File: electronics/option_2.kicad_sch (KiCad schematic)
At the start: 11 parts, among them Q6 Q_PMOS_GSD, U19 LM339_4ch, U20 LM339_4ch, U5 ULN2801A

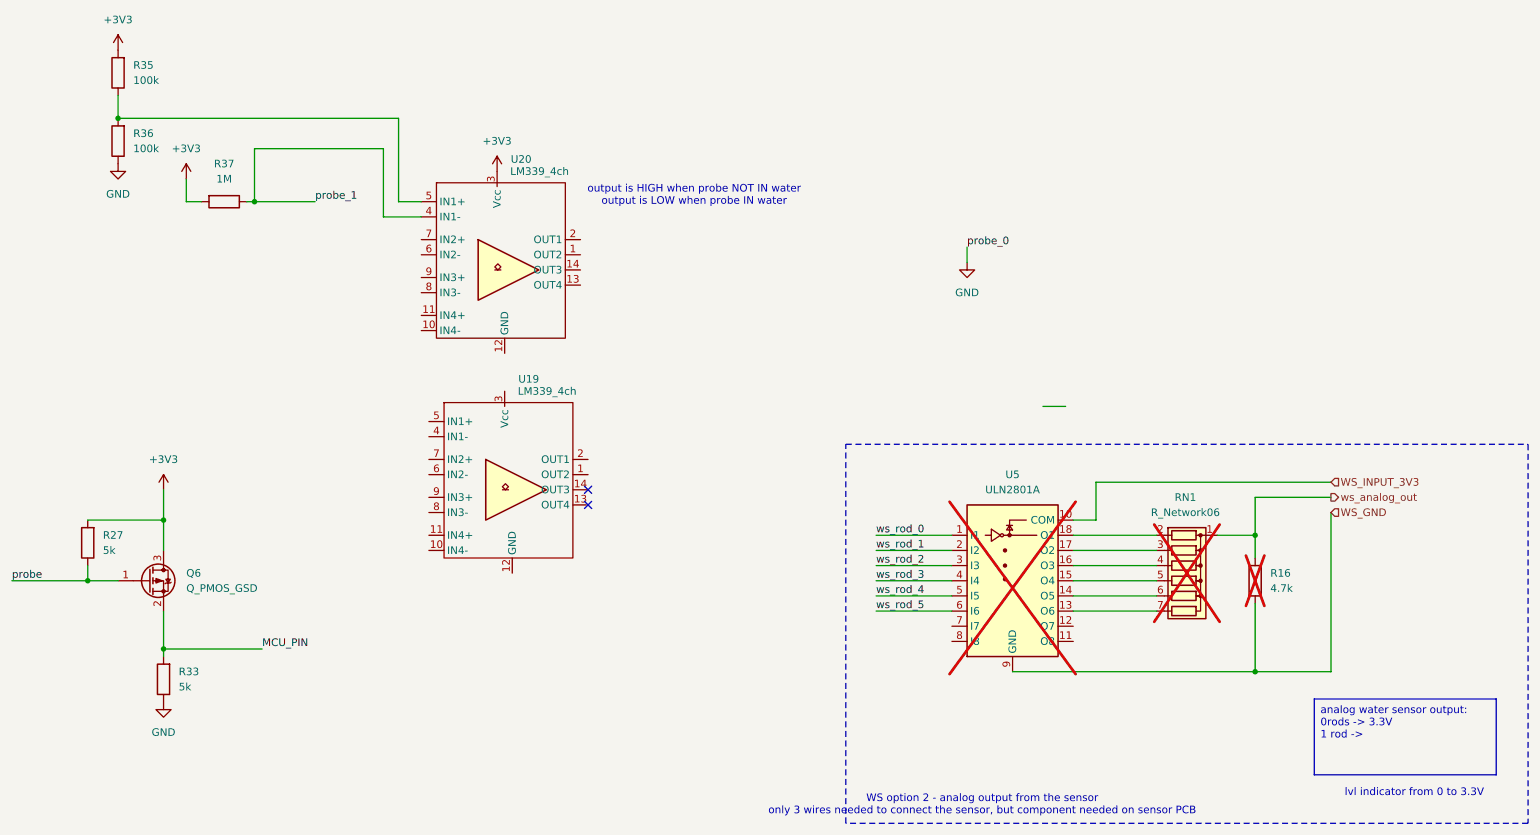
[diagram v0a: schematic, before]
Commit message: start to create BOM and finalising symbol fields
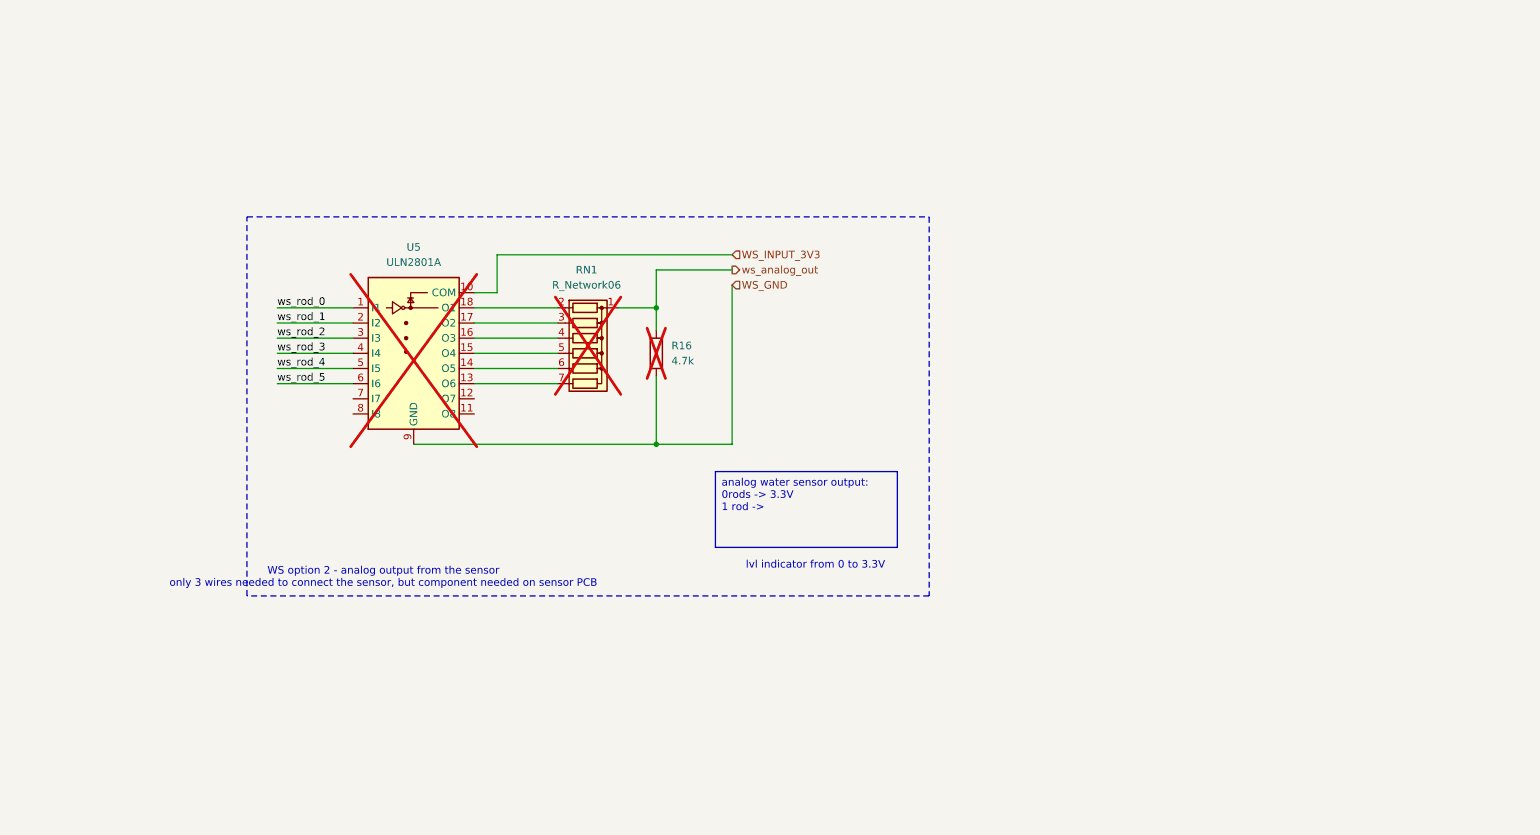
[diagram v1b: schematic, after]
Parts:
- removed Q6: Q_PMOS_GSD, symbol Device:Q_PMOS_GSD
- removed R27, R33: 5k, Resistor_SMD:R_0805_2012Metric_Pad1.20x1.40mm_HandSolder, symbol Device:R
- removed R35, R36: 100k, Resistor_SMD:R_0805_2012Metric_Pad1.20x1.40mm_HandSolder, symbol Device:R
- removed R37: 1M, Resistor_SMD:R_0805_2012Metric_Pad1.20x1.40mm_HandSolder, symbol Device:R
- removed U19: LM339_4ch, Package_SO:HTSSOP-14-1EP_4.4x5mm_P0.65mm_EP3.4x5mm_Mask3x3.1mm_ThermalVias, symbol HeavyDuty:LM339_4ch
- removed U20: LM339_4ch, Package_SO:SOIC-14W_7.5x9mm_P1.27mm, symbol HeavyDuty:LM339_4ch
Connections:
- no-connect marks 2 -> 0
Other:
- note removed: "output is HIGH when probe NOT IN water output is LOW when probe IN water"
- moved on the sheet: R16, RN1, U5

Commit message: nerd weekend update
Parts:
- added R35, R36: 100k, symbol Device:R
- added R37: 1M, symbol Device:R
- added U19, U20: LM339_4ch, Package_SO:HTSSOP-14-1EP_4.4x5mm_P0.65mm_EP3.4x5mm_Mask3x3.1mm_ThermalVias, symbol HeavyDuty:LM339_4ch
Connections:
- new net: R35.1, R36.2, U20.5 (IN1+)
- new net +3V3: R35.2, R37.2, U20.3 (Vcc)
- new net GND: R36.1
- new net probe_1: R37.1, U20.4 (IN1-)
- no-connect marks 0 -> 2
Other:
- note added: "output is HIGH when probe NOT IN water output is LOW when probe IN water"
- moved on the sheet: R16, RN1, U5
